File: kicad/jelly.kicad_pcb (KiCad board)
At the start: 2 copper layers, 59.9 x 32.9 mm, 45 parts, among them M1 PAGER_MOTOR, M2 PAGER_MOTOR, P1 CONN_01X01, P10 CONN_01X01, P11 CONN_01X01, P12 CONN_01X01, P13 CONN_01X01, P14 CONN_01X01, P15 CONN_01X01, P2 CONN_01X01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

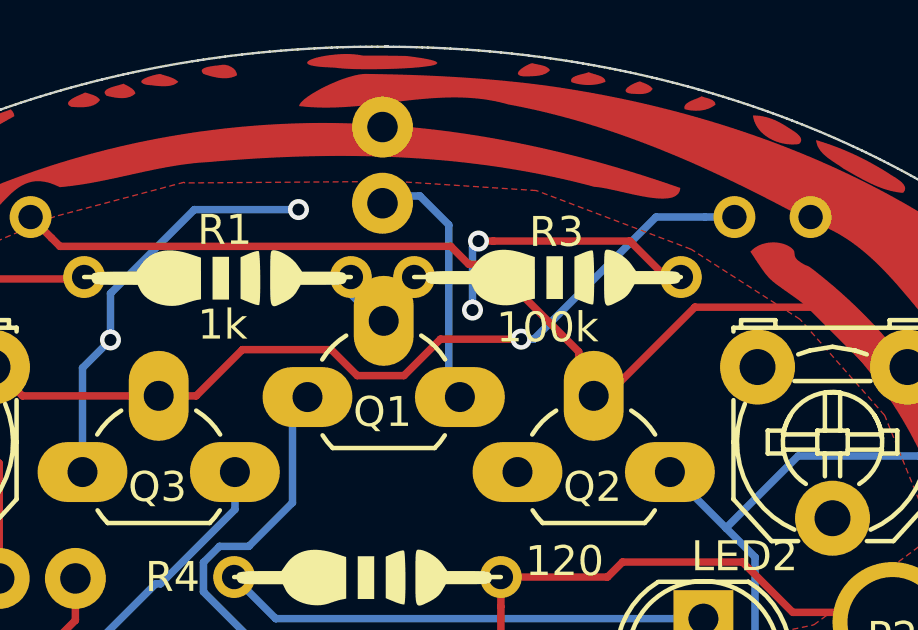
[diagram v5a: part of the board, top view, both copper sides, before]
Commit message: Move LDR drawings
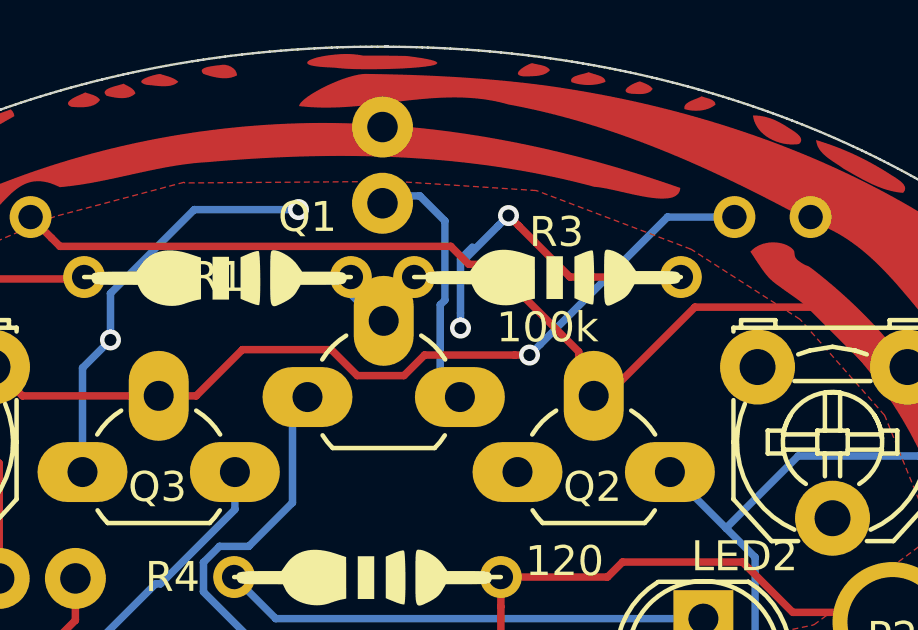
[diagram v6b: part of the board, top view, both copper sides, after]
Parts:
- moved DNP2 3.44 mm to (156.7, 71.8)
- moved DNP3 3.27 mm to (143.5, 71.8)
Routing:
- net GND: track 74.8 -> 76.7 mm

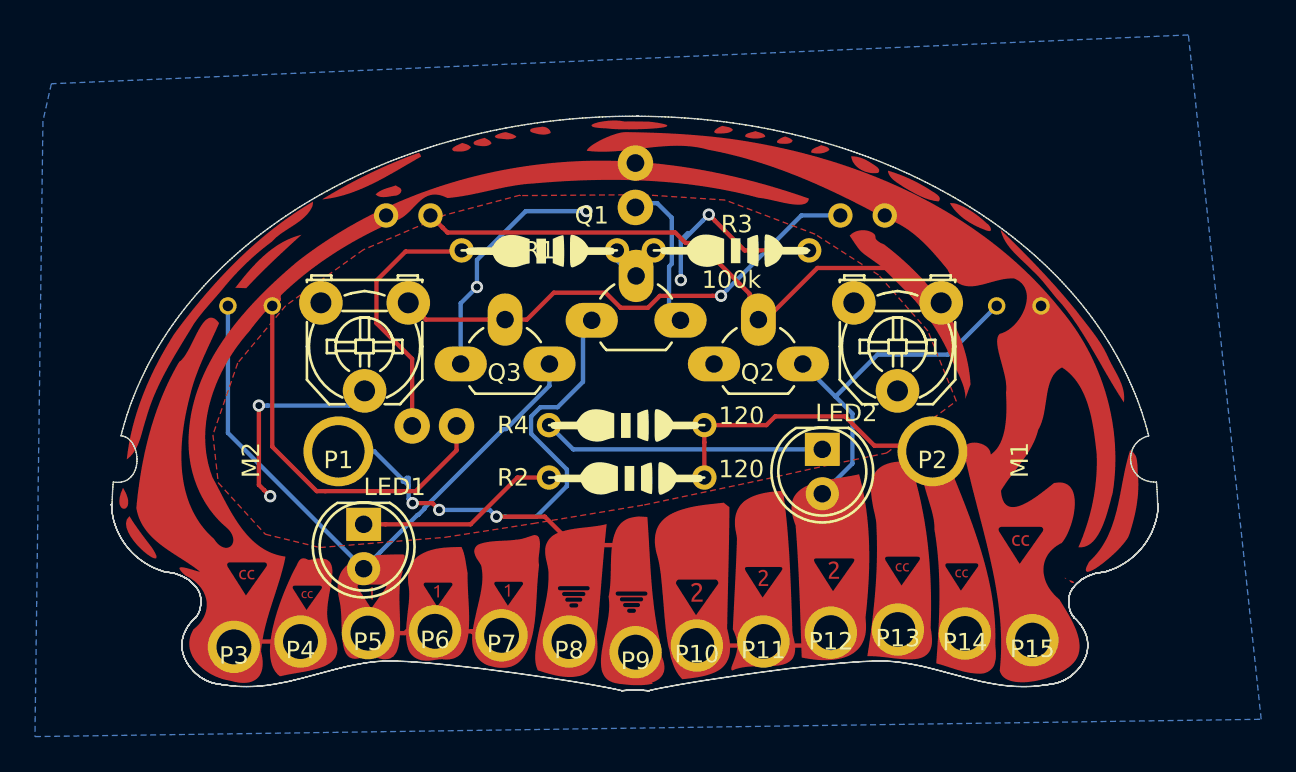
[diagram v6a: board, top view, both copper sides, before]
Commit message: Delete traces and make things more symmetrical
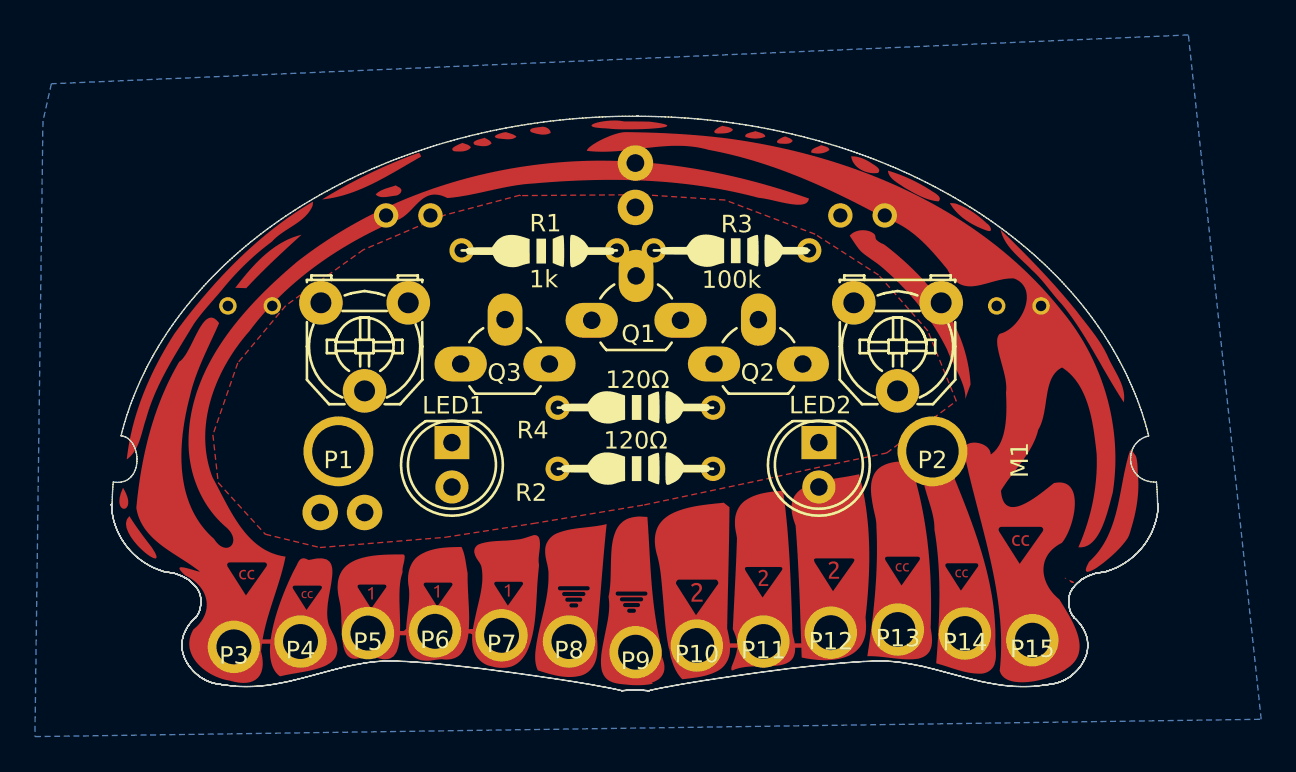
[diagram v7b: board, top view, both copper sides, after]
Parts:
- R2, R4: value 120 -> 120Ω
- moved LED1 6.89 mm to (139.6, 82.8)
- moved SW1 5.65 mm to (134.6, 86.8), turned to 90 degrees
- moved DNP6 1.20 mm to (150.1, 80.8)
- moved R4 1.12 mm to (150.1, 80.8)
- moved R2 0.71 mm to (150.1, 84.3)
- moved DNP9 0.69 mm to (150.1, 84.3)
- moved LED2 0.43 mm to (160.6, 82.8)
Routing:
- net GND: track 76.7 -> 1.08 mm, vias 9 -> 0
- net VCC: track 55.6 -> 3.94 mm
- net Net-(PHOTO2-Pad1): track 34.6 -> 0.00 mm
- net Vout1: track 43.1 -> 8.63 mm
- net Net-(PHOTO1-Pad1): track 28.3 -> 0.00 mm, vias 1 -> 0
- net Vout2: track 29.9 -> 7.98 mm
- net Net-(LED2-Pad1): track 16.2 -> 0.00 mm
- net Net-(R1-Pad1): track 14.3 -> 0.00 mm
- net Net-(LED1-Pad1): track 11.7 -> 0.00 mm
- net Net-(BT1-Pad2): track 8.91 -> 0.00 mm
- net Net-(Q1-Pad2): track 3.82 -> 0.00 mm
